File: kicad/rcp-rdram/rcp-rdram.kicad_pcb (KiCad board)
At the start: 2 copper layers, 36.8 x 54.6 mm, 29 parts, among them P1 RDRAM-EDGE, U11 RDRAM18-NUS, U11-2 RDRAM18-NUS, U14 RDRAM18-NUS, U14-2 RDRAM18-NUS, U15 MX8330, X2 14.705MHz

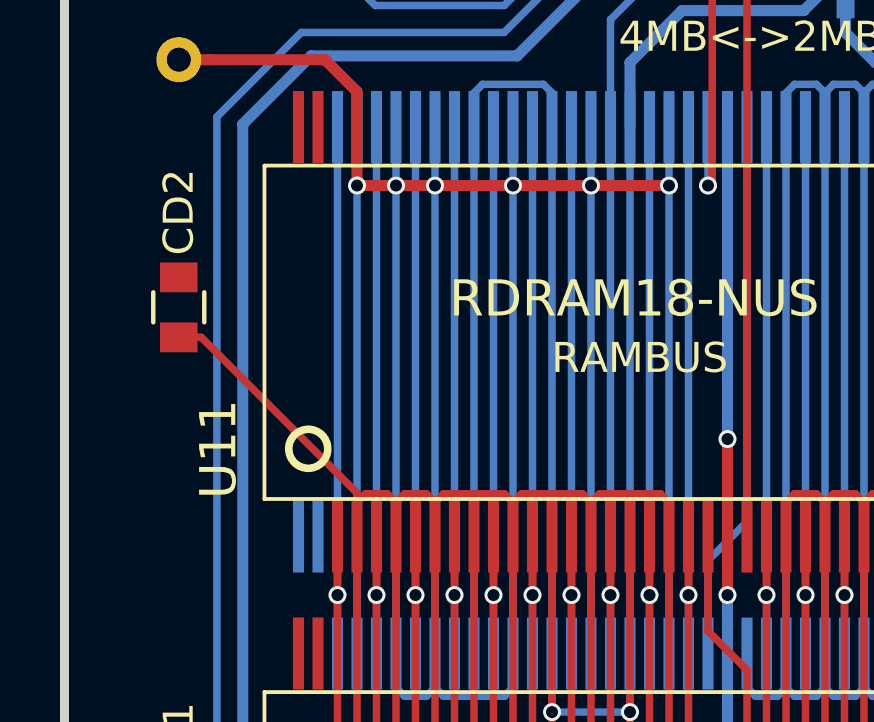
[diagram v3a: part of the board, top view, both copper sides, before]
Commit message: Fixed GND connections to top side RAM chips
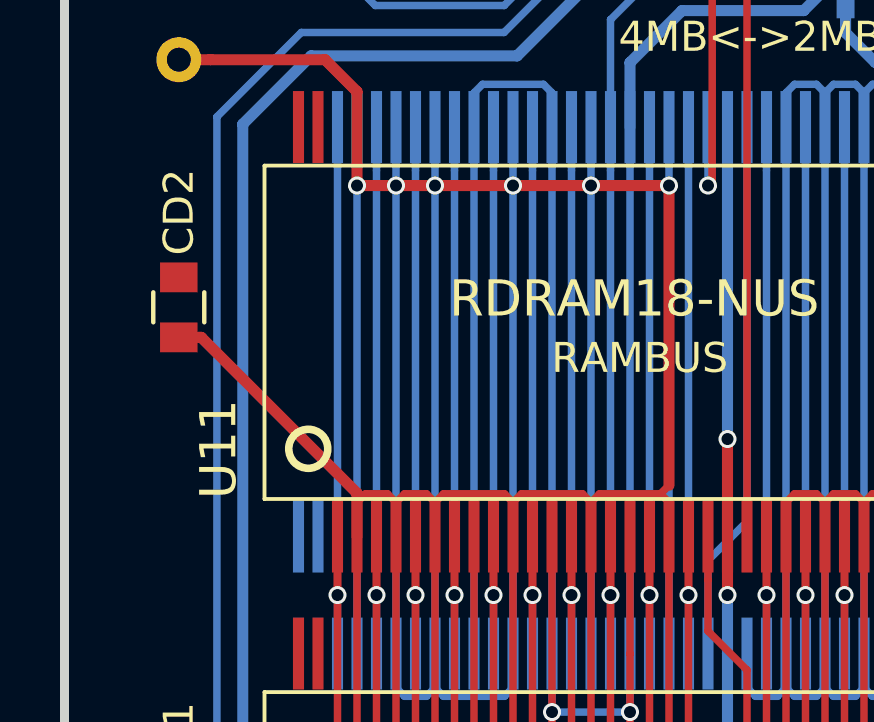
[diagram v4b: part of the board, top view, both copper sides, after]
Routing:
- net GND: track 556.9 -> 567.3 mm
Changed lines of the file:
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@@
   (general
     (links 199)
-    (no_connects 3)
-    (area 101.449999 76.049999 138.580001 130.960001)
+    (no_connects 2)
+    (area 91.095714 75.765 150.204286 133.510001)
     (thickness 1.6)
     (drawings 13)
-    (tracks 475)
+    (tracks 477)
     (zones 0)
     (modules 29)
@@
   (segment (start 123.7 111.934829) (end 123.686323 111.948506) (width 0.37) (layer B.Cu) (net 1))
   (segment (start 123.386324 112.248505) (end 123.686323 111.948506) (width 0.37) (layer B.Cu) (net 1))
+  (via (at 108.767764 116.77007) (size 0.6) (drill 0.4) (layers F.Cu B.Cu) (net 1))
+  (segment (start 106.553 123.047) (end 106.553 118.984834) (width 0.37) (layer F.Cu) (net 1))
+  (segment (start 106.553 118.984834) (end 108.467765 117.070069) (width 0.37) (layer F.Cu) (net 1))
+  (segment (start 108.467765 117.070069) (end 108.767764 116.77007) (width 0.37) (layer F.Cu) (net 1))
+  (segment (start 118.864759 116.77007) (end 123.386324 112.248505) (width 0.37) (layer B.Cu) (net 1))
   (segment (start 108.767764 116.77007) (end 118.864759 116.77007) (width 0.37) (layer B.Cu) (net 1))
   (segment (start 124.593228 112.855411) (end 123.986322 112.248505) (width 0.37) (layer B.Cu) (net 1))
-  (segment (start 118.864759 116.77007) (end 123.386324 112.248505) (width 0.37) (layer B.Cu) (net 1))
   (segment (start 123.986322 112.248505) (end 123.686323 111.948506) (width 0.37) (layer B.Cu) (net 1))
   (segment (start 134.483833 112.855411) (end 124.593228 112.855411) (width 0.37) (layer B.Cu) (net 1))
@@
   (segment (start 135.765 95.52) (end 134.483833 96.801167) (width 0.37) (layer F.Cu) (net 1))
   (via (at 134.483833 112.855411) (size 0.6) (drill 0.4) (layers F.Cu B.Cu) (net 1))
-  (segment (start 108.467765 117.070069) (end 108.767764 116.77007) (width 0.37) (layer F.Cu) (net 1))
-  (segment (start 106.553 118.984834) (end 108.467765 117.070069) (width 0.37) (layer F.Cu) (net 1))
-  (segment (start 106.553 123.047) (end 106.553 118.984834) (width 0.37) (layer F.Cu) (net 1))
-  (via (at 108.767764 116.77007) (size 0.6) (drill 0.4) (layers F.Cu B.Cu) (net 1))
   (segment (start 106.553 123.047) (end 106.41 123.19) (width 0.25) (layer F.Cu) (net 1))
   (segment (start 135.765 95.52) (end 135.89 95.52) (width 0.25) (layer F.Cu) (net 1))
@@
   (segment (start 129.424999 129.070001) (end 130.545 127.95) (width 0.37) (layer F.Cu) (net 1))
   (segment (start 130.545 127.95) (end 131.445 127.95) (width 0.37) (layer F.Cu) (net 1))
+  (segment (start 121.75 92.46) (end 121.75 102.45) (width 0.37) (layer F.Cu) (net 2))
+  (segment (start 121.75 102.45) (end 121.465001 102.734999) (width 0.25) (layer F.Cu) (net 2))
+  (segment (start 111.349999 121.710001) (end 111.349999 104.16) (width 0.25) (layer F.Cu) (net 2))
+  (segment (start 116.549999 121.710001) (end 116.549999 104.16) (width 0.25) (layer F.Cu) (net 2))
   (segment (start 113.949999 108.059999) (end 113.949999 109.200001) (width 0.25) (layer B.Cu) (net 2))
   (segment (start 113.949999 109.200001) (end 114.234998 109.485) (width 0.25) (layer B.Cu) (net 2))
@@
   (segment (start 111.634998 102.734999) (end 112.365 102.734999) (width 0.25) (layer F.Cu) (net 2))
   (segment (start 112.365 102.734999) (end 112.649999 103.019998) (width 0.25) (layer F.Cu) (net 2))
-  (segment (start 111.349999 104.16) (end 111.349999 102.71) (width 0.25) (layer F.Cu) (net 2))
-  (segment (start 111.349999 102.71) (end 106.159999 97.52) (width 0.25) (layer F.Cu) (net 2))
-  (segment (start 106.159999 97.52) (end 105.41 97.52) (width 0.25) (layer F.Cu) (net 2))
+  (segment (start 111.349999 104.16) (end 111.349999 102.71) (width 0.37) (layer F.Cu) (net 2))
+  (segment (start 106.159999 97.52) (end 105.41 97.52) (width 0.37) (layer F.Cu) (net 2))
+  (segment (start 111.349999 102.71) (end 106.159999 97.52) (width 0.37) (layer F.Cu) (net 2))
   (segment (start 136.015 115.3) (end 137.583563 113.731437) (width 0.37) (layer F.Cu) (net 2))
   (segment (start 136.639999 106.159999) (end 135.89 105.41) (width 0.37) (layer F.Cu) (net 2))
@@
   (segment (start 129.55 108.059999) (end 129.55 90.51) (width 0.25) (layer B.Cu) (net 2))
   (segment (start 130.2 90.51) (end 130.2 108.059999) (width 0.25) (layer B.Cu) (net 2))
-  (segment (start 111.349999 121.710001) (end 111.349999 104.16) (width 0.25) (layer F.Cu) (net 2))
   (segment (start 112.649999 121.710001) (end 112.649999 104.16) (width 0.25) (layer F.Cu) (net 2))
   (segment (start 113.949999 121.710001) (end 113.949999 104.16) (width 0.25) (layer F.Cu) (net 2))
-  (segment (start 116.549999 121.710001) (end 116.549999 104.16) (width 0.25) (layer F.Cu) (net 2))
   (segment (start 121.75 121.710001) (end 121.75 104.16) (width 0.25) (layer F.Cu) (net 2))
   (segment (start 125.65 121.710001) (end 125.65 104.16) (width 0.25) (layer F.Cu) (net 2))

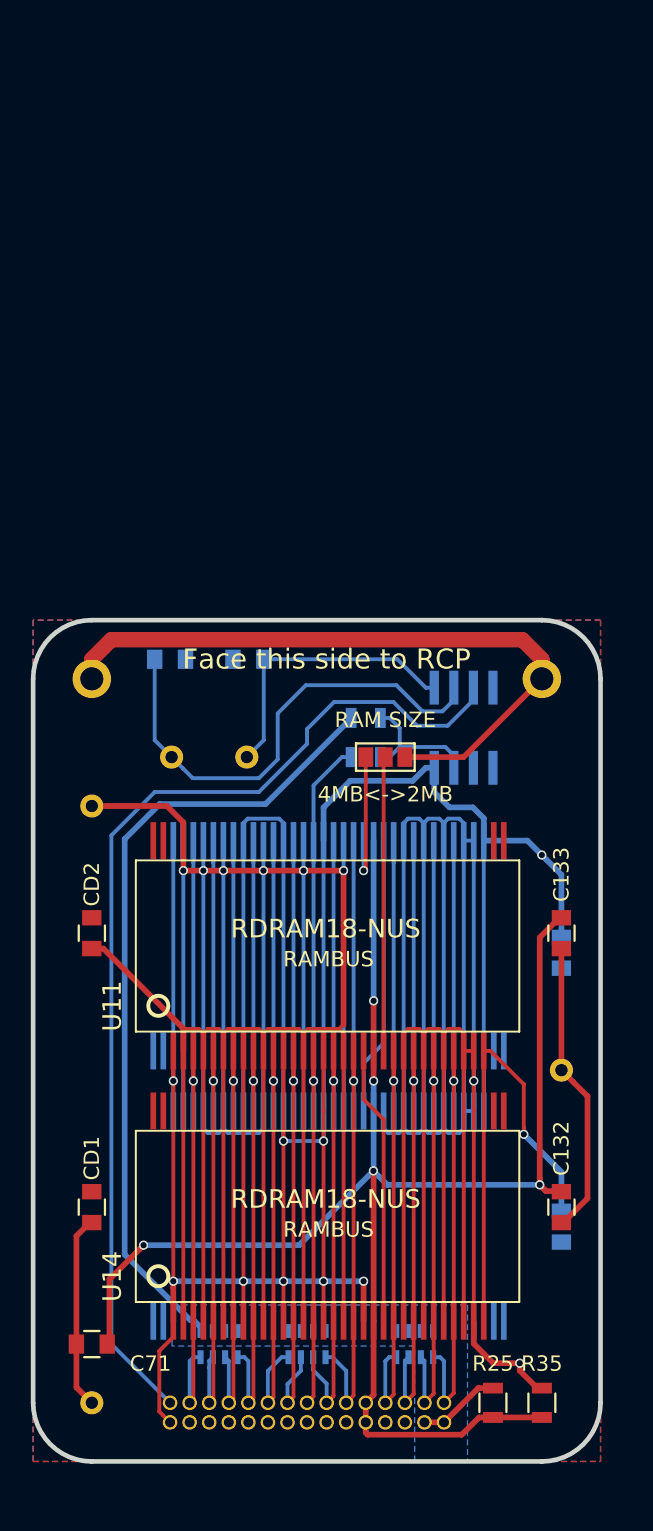
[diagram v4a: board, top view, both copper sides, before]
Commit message: Adjusted track clearance to minimum of 0.15mm according to my PCB house design rules for better pricing
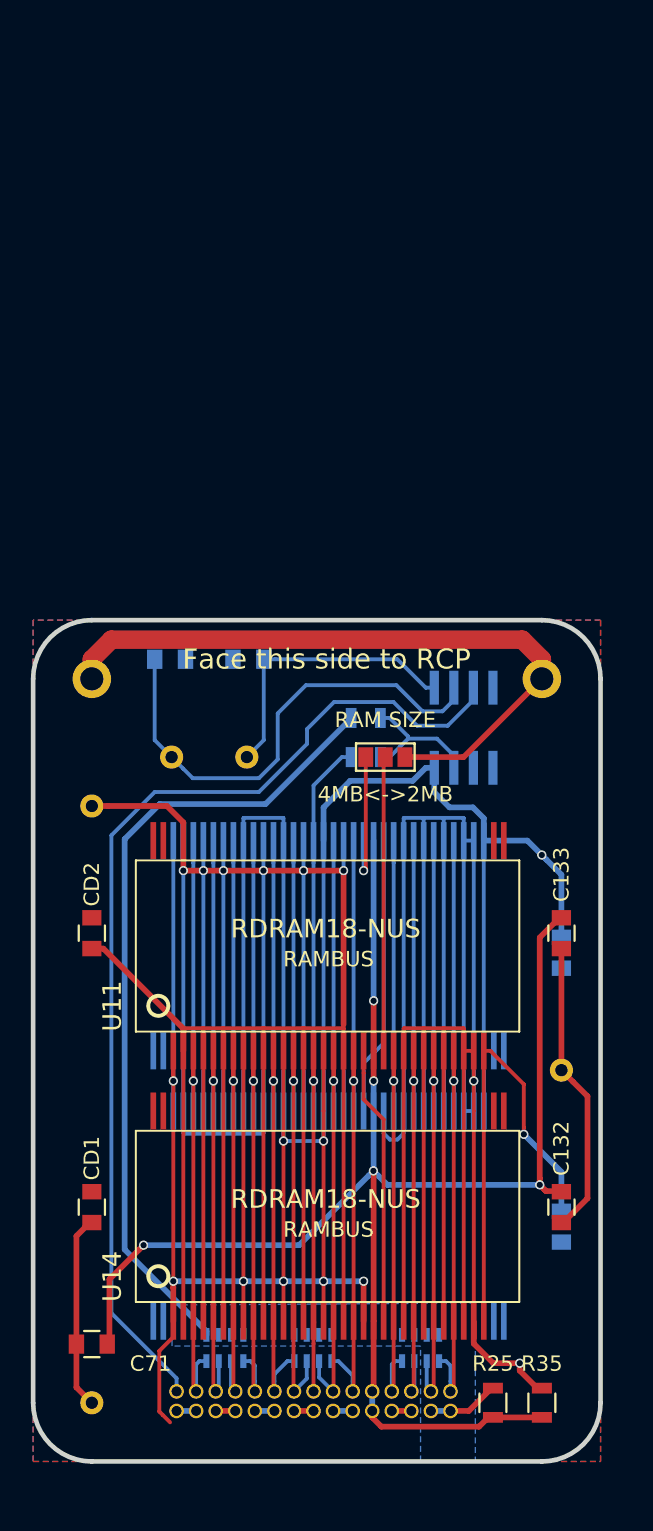
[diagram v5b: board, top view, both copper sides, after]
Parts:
- moved P1 0.85 mm to (128.7, 126.3)
- moved RA1 0.46 mm to (114.0, 123.4)
- moved RA2 0.46 mm to (119.8, 123.4)
- moved RA3 0.46 mm to (126.7, 123.4)
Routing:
- net VDD: track 254.0 -> 258.2 mm
- net GND: track 567.3 -> 569.7 mm
- net /DQ3: track 46.1 -> 44.2 mm
- net /DQ2: track 45.6 -> 43.7 mm
- net /RXCLK: track 45.8 -> 43.9 mm
- net /DQ4: track 45.9 -> 44.0 mm
- net /DQ1: track 45.6 -> 43.8 mm
- net /DQ0: track 46.1 -> 44.2 mm
- net /COMMAND: track 46.3 -> 44.4 mm
- net /DQ5: track 46.3 -> 44.4 mm
- net /DQ6: track 46.0 -> 44.2 mm
- net /DQ7: track 45.5 -> 43.7 mm
- net /ADDRESS: track 45.5 -> 43.7 mm
- net /DQ8: track 46.0 -> 44.2 mm
- net /VREF: track 105.7 -> 104.1 mm
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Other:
- net class Default: clearance 0.1 -> 0.15
- net class Power added: clearance 0.1, trace_width 0.37, via_dia 0.6, via_drill 0.4
- rule trace_clearance: 0.1 -> 0.15
- board text added: "N64 RAM board v1.3"

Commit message: Cleanups, DRC passed
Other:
- net class Power: clearance 0.1 -> 0.15
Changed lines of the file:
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@@
     (links 199)
     (no_connects 0)
-    (area 91.045714 75.715 150.254286 133.510001)
+    (area 101.449999 76.049999 138.580001 130.960001)
     (thickness 1.6)
     (drawings 14)
@@
   )
   (net_class Power ""
-    (clearance 0.1)
+    (clearance 0.15)
     (trace_width 0.37)
     (via_dia 0.6)
